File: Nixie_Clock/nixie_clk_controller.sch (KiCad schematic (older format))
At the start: 2 parts

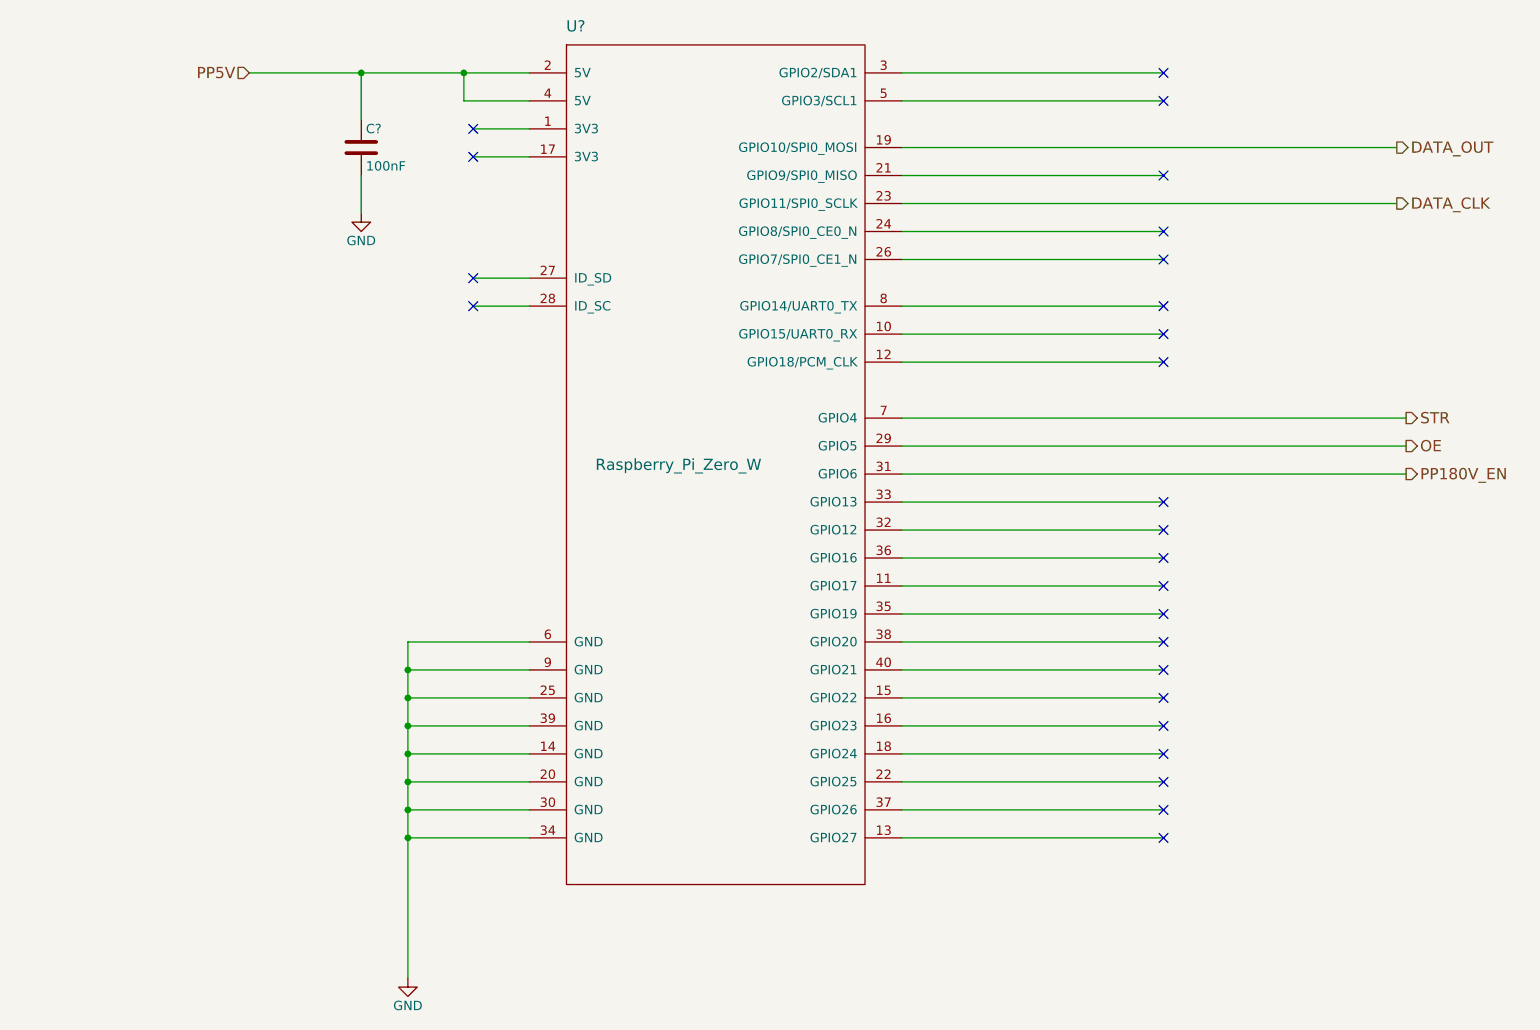
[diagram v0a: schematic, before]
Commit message: Added PIC16 instead of RaspBerry PI
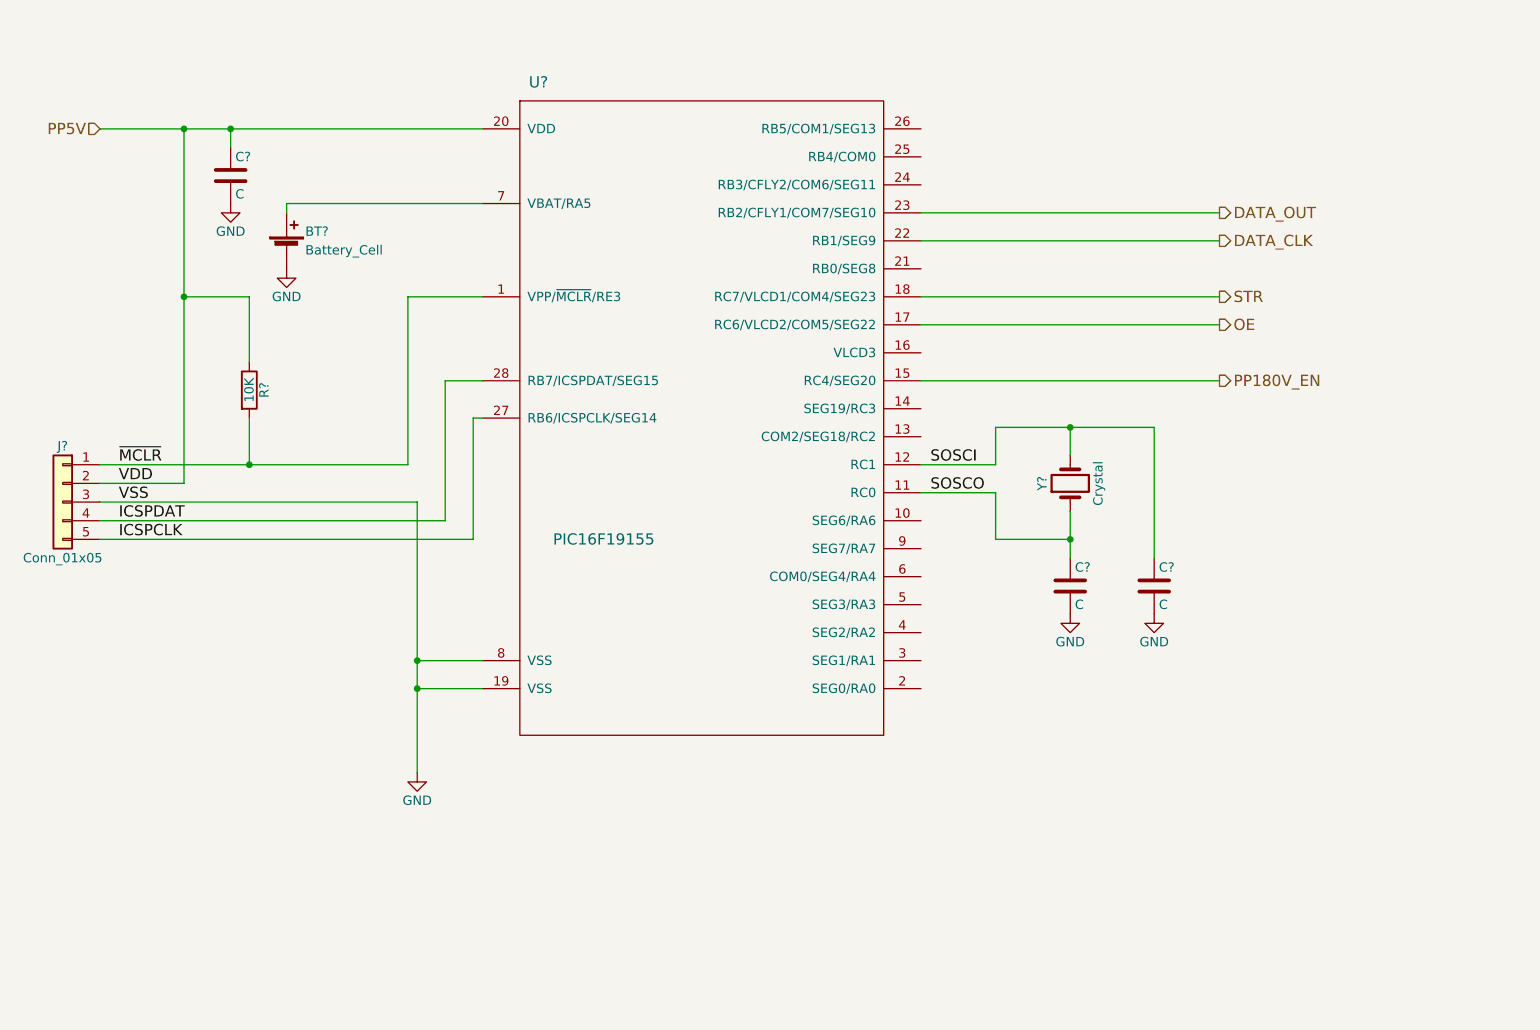
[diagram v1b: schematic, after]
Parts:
- removed C?: 100nF, symbol C
- removed U?: Raspberry_Pi_Zero_W, symbol Raspberry_Pi_Zero_W
- added BT?: Battery_Cell, symbol Battery_Cell
- added C? (x3): C, symbol C
- added J?: Conn_01x05, symbol Conn_01x05
- added R?: 10K, symbol R
- added U?: PIC16F19155, symbol PIC16F19155
- added Y?: Crystal, symbol Crystal
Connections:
- net DATA_CLK: now also U?.22 (RB1/SEG9)
- net DATA_OUT: now also U?.23 (RB2/CFLY1/COM7/SEG10)
- net GND: now also BT?.2 (-), C?.2, C?.2, C?.2, J?.3 (Pin_3), U?.19 (VSS), U?.8 (VSS)
- net OE: now also U?.17 (RC6/VLCD2/COM5/SEG22)
- net PP180V_EN: now also U?.15 (RC4/SEG20)
- net PP5V: now also C?.1, J?.2 (Pin_2), R?.1, U?.20 (VDD)
- net STR: now also U?.18 (RC7/VLCD1/COM4/SEG23)
- new net: BT?.1 (+), U?.7 (VBAT/RA5)
- new net ICSPCLK: J?.5 (Pin_5), U?.27 (RB6/ICSPCLK/SEG14)
- new net ICSPDAT: J?.4 (Pin_4), U?.28 (RB7/ICSPDAT/SEG15)
- new net SOSCI: C?.1, U?.12 (RC1), Y?.2
- new net SOSCO: C?.1, U?.11 (RC0), Y?.1
- new net ~MCLR: J?.1 (Pin_1), R?.2, U?.1 (VPP/~MCLR~/RE3)
- no-connect marks 25 -> 0
